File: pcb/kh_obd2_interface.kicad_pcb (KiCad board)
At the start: 2 copper layers, 35 parts, among them J1 OBD2, J2 CAN, Q201 CSD18540Q5B, U1 STM32G0B1RET6, U201 LM74500-Q1, U202 TVS2700DRV, U3 TPSM33620S5QRDNRQ1, U301 TCAN3403-Q1, U4 LM1117-Q1-3.3

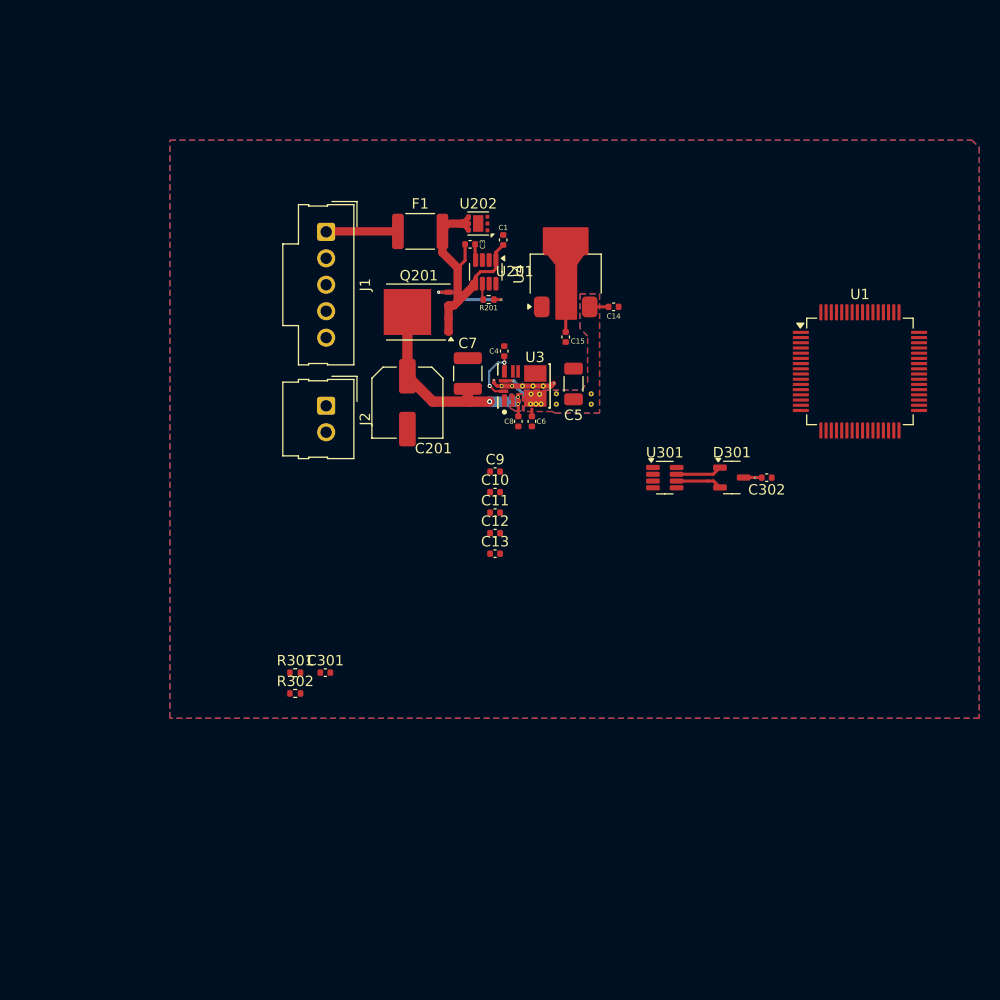
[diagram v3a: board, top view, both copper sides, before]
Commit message: add transceivers, routing, drc
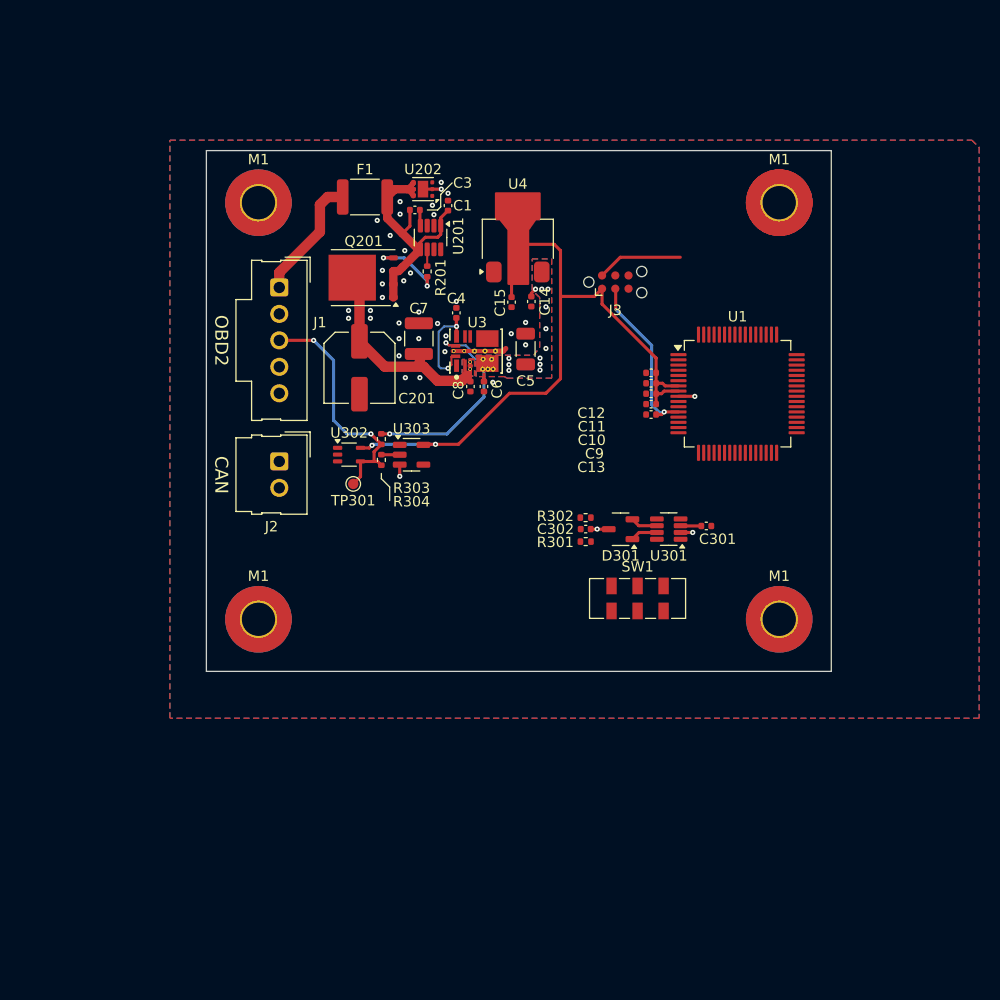
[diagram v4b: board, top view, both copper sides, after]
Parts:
- removed the ? at (54.5, 39.4)
- removed the ? at (51.1, 39.4)
- removed the ? at (54.5, 38.4)
- removed the ? at (51.1, 38.4)
- added ?: , , F.Cu at (72.5, 20.0)
- added J3: TC2030, Connector:Tag-Connect_TC2030-IDC-NL_2x03_P1.27mm_Vertical, F.Cu at (56.8, 27.6)
- added M1: MountingHole_3.2mm_M3_Pad_TopBottom, MountingHole:MountingHole_3.2mm_M3_Pad_TopBottom, F.Cu at (72.5, 60.0)
- added M1: MountingHole_3.2mm_M3_Pad_TopBottom, MountingHole:MountingHole_3.2mm_M3_Pad_TopBottom, F.Cu at (22.5, 60.0)
- added M1: MountingHole_3.2mm_M3_Pad_TopBottom, MountingHole:MountingHole_3.2mm_M3_Pad_TopBottom, F.Cu at (22.5, 20.0)
- added M1: MountingHole_3.2mm_M3_Pad_TopBottom, MountingHole:MountingHole_3.2mm_M3_Pad_TopBottom, F.Cu at (72.5, 20.0)
- added R303: 510r, Resistor_SMD:R_0402_1005Metric, F.Cu at (34.3, 42.7)
- added R304: 33r, Resistor_SMD:R_0402_1005Metric, F.Cu at (34.3, 44.7)
- added SW1: TermSw, Button_Switch_SMD:SW_DPDT_CK_JS202011JCQN, F.Cu at (58.9, 58.0)
- added TP301: HLine, TestPoint:TestPoint_Pad_D1.0mm, F.Cu at (31.6, 47.0)
- added U302: 74LVC1G07, Package_TO_SOT_SMD:Texas_R-PDSO-G5_DCK-5, F.Cu at (31.2, 44.2)
- added U303: SN74LV1T34DBV, Package_TO_SOT_SMD:SOT-23-5, F.Cu at (37.2, 44.2)
- moved C301 39.2 mm to (65.5, 51.0), turned to 180 degrees
- moved R302 32.6 mm to (53.9, 50.2)
- moved R301 30.6 mm to (53.9, 52.5), turned to 180 degrees
- moved C12 21.5 mm to (60.2, 36.3), turned to 180 degrees
- moved C13 20.1 mm to (60.2, 40.3)
- moved C11 19.5 mm to (60.2, 37.3), turned to 180 degrees
- moved C302 18.1 mm to (53.9, 51.3), turned to 0 degrees
- moved C10 17.7 mm to (60.2, 38.3), turned to 180 degrees
- moved C9 16.3 mm to (60.2, 39.3), turned to 180 degrees
- moved U1 11.9 mm to (68.5, 38.3)
- moved D301 11.8 mm to (57.3, 51.4), turned to 180 degrees
- moved C14 7.92 mm to (48.7, 29.5), turned to -90 degrees
- moved J2 6.98 mm to (24.5, 44.8)
- moved J1 6.98 mm to (24.5, 28.1)
- moved R201 6.49 mm to (38.7, 26.6), turned to 90 degrees
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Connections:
- net /MCU/MCU_NRST renamed /Connectors/MCU_NRST
- net /Transceivers/RX renamed /MCU/RX
- net /Transceivers/STB renamed /MCU/STB
- net /Transceivers/TX renamed /MCU/TX
- C15 pad 1: +3.3V -> +3V3
- C3 pad 1: +BATT_FUSED -> /Power/BATT_FUSED
- C301 pad 2: +3.3V -> +3V3
- J2 pad 1: unconnected-(J2-Pin_1-Pad1) -> /Connectors/CAN1.H
- J2 pad 2: unconnected-(J2-Pin_2-Pad2) -> /Connectors/CAN1.L
- R301 pad 2: Net-(C302-Pad1) -> Net-(R301-Pad2)
- R302 pad 1: Net-(C302-Pad1) -> Net-(R302-Pad1)
- U1 pad 45: /MCU/MCU_SWDIO -> /Connectors/MCU_SWDIO
- U1 pad 46: /MCU/MCU_SWCLK_BOOT0 -> /Connectors/MCU_SWCLK_BOOT0
- U201 pad 1: +BATT_FUSED -> /Power/BATT_FUSED
- U301 pad 3: +3.3V -> +3V3
- U4 pad 2: +3.3V -> +3V3
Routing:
- net +3V3: track 0.00 -> 68.8 mm, vias 0 -> 2
- net /Connectors/H Line: track 0.00 -> 23.7 mm, vias 0 -> 2
- net /Connectors/MCU_NRST: track 0.00 -> 16.4 mm, vias 0 -> 2
- net +5V: track 6.21 -> 21.0 mm, vias 1 -> 14
- net /Connectors/MCU_SWDIO: track 0.00 -> 8.23 mm
- net +BATT: track 6.91 -> 12.1 mm
- net +3.3V: track 5.12 -> 0.00 mm
- net GND: track 8.42 -> 12.4 mm, vias 3 -> 38
- net Net-(U3-MODE/SYNC): track 6.21 -> 9.67 mm
- net /Transceivers/CAN1.L: track 4.42 -> 2.60 mm
- net /Transceivers/CAN1.H: track 4.43 -> 2.61 mm
- net Net-(U303-A): track 0.00 -> 1.77 mm
- net /Power/BATT_FUSED: track 26.0 -> 25.2 mm
- net +12V: track 20.4 -> 20.8 mm, vias 1 -> 0
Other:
- board outline added: 60 x 50 mm
- board text added: "CAN"
- board text added: "OBD2"

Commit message: busses are hard
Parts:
- added J3: USB-C 2.0, Connector_USB:USB_C_Receptacle_GCT_USB4105-xx-A_16P_TopMnt_Horizontal, F.Cu at (60.3, 18.7)
- added J4: RTC_BAT, Connector_Molex:Molex_PicoBlade_53047-0210_1x02_P1.25mm_Vertical, F.Cu at (72.8, 51.2)
- added R401: 5.1k, Resistor_SMD:R_0402_1005Metric, F.Cu at (61.8, 24.5)
- added R402: 5.1k, Resistor_SMD:R_0402_1005Metric, F.Cu at (58.8, 24.5)
- added SW2: SW_SPDT, Connector_PinHeader_2.54mm:PinHeader_1x03_P2.54mm_Vertical_SMD_Pin1Left, F.Cu at (47.6, 27.7)
- moved J_SWD1 16.3 mm to (73.0, 26.7)
- moved C15 13.1 mm to (53.0, 18.0), turned to 90 degrees
- moved C14 8.77 mm to (42.7, 23.1)
- moved SW1 5.40 mm to (53.5, 57.3)
- moved C5 3.36 mm to (47.7, 37.4), turned to 90 degrees
- moved U4 3.16 mm to (47.7, 20.4), turned to 0 degrees
- renumbered J3 to J_SWD1
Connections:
- net /MCU/KL_UART.RX renamed /MCU/KLINE.RX
- net /MCU/KL_UART.TX renamed /MCU/KLINE.TX
- C5 pad 2: +5V -> /Power/CAR_5V
- C6 pad 2: +5V -> /Power/CAR_5V
- D301 pad 1: /Transceivers/CAN1.H -> /Connectors/H_+
- D301 pad 2: /Transceivers/CAN1.L -> /Connectors/L_-
- J2 pad 1: /Connectors/CAN1.H -> /Connectors/H_+
- J2 pad 2: /Connectors/CAN1.L -> /Connectors/L_-
- R301 pad 1: /Transceivers/CAN1.H -> /Connectors/H_+
- R302 pad 2: /Transceivers/CAN1.L -> /Connectors/L_-
- U1 pad 19: /MCU/HL_UART.TX -> /MCU/HLINE.TX
- U1 pad 20: /MCU/HL_UART.RX -> /MCU/HLINE.RX
- U1 pad 40: unconnected-(U1-PD8-Pad40) -> /MCU/TX
- U1 pad 41: unconnected-(U1-PD9-Pad41) -> /MCU/RX
- U1 pad 43: /MCU/USB1.DM -> /Connectors/DN
- U1 pad 44: /MCU/USB1.DP -> /Connectors/DP
- U1 pad 6: /MCU/RTC_VBAT -> /Connectors/RTC_VBAT
- U3 pad 4: +5V -> /Power/CAR_5V
- U3 pad 9: +5V -> /Power/CAR_5V
- U301 pad 6: /Transceivers/CAN1.L -> /Connectors/L_-
- U301 pad 7: /Transceivers/CAN1.H -> /Connectors/H_+
- U302 pad 2: /Transceivers/HL_UART.TX -> /MCU/HLINE.TX
- U303 pad 4: /Transceivers/HL_UART.RX -> /MCU/HLINE.RX
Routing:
- net /Connectors/DN: track 0.00 -> 31.7 mm
- net /Connectors/DP: track 0.00 -> 28.7 mm, vias 0 -> 2
- net /Connectors/RTC_VBAT: track 0.00 -> 20.6 mm
- net /Power/CAR_5V: track 0.00 -> 19.8 mm, vias 0 -> 2
- net /Connectors/USB_5V: track 0.00 -> 19.3 mm, vias 0 -> 2
- net +5V: track 21.0 -> 1.82 mm, vias 14 -> 0
- net +3V3: track 68.8 -> 51.3 mm, vias 2 -> 3
- net /Connectors/MCU_NRST: track 16.4 -> 2.25 mm, vias 2 -> 1
- net /Connectors/MCU_SWDIO: track 8.23 -> 0.00 mm
- net /Connectors/H_+: track 0.00 -> 7.20 mm
- net /Connectors/L_-: track 0.00 -> 5.97 mm
- net /Transceivers/CAN1.H: track 2.61 -> 0.00 mm
- net /Transceivers/CAN1.L: track 2.60 -> 0.00 mm
- net Net-(J3-CC2): track 0.00 -> 1.71 mm
- net Net-(J3-CC1): track 0.00 -> 1.71 mm
- added copper zone on B.Cu, net /Power/CAR_5V
- added copper zone on F.Cu, net /Power/CAR_5V
- removed copper zone on B.Cu, net +5V
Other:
- board text added: "CAR"
- board text added: "USB"

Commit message: Add TLIN2027, placement, DRC fixes, routing
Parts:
- removed ?: , 
- removed SW1: TermSw, Button_Switch_SMD:SW_DPDT_CK_JS202011JCQN
- added JP1: SolderJumper_2_Open, Jumper:SolderJumper-2_P1.3mm_Open_RoundedPad1.0x1.5mm, F.Cu at (52.0, 91.7)
- added JP2: SolderJumper_2_Open, Jumper:SolderJumper-2_P1.3mm_Open_RoundedPad1.0x1.5mm, F.Cu at (52.1, 85.8)
- added R305: 5.1k, Resistor_SMD:R_0402_1005Metric, F.Cu at (42.9, 43.8)
- added U2: TLIN2027-Q1, Package_SO:SOIC-8_3.9x4.9mm_P1.27mm, F.Cu at (48.1, 44.4)
- moved C301 37.4 mm to (63.6, 88.4)
- moved R301 37.4 mm to (52.1, 89.9)
- moved R302 37.4 mm to (52.1, 87.6)
- moved C302 37.4 mm to (52.1, 88.7)
- moved U301 37.4 mm to (60.0, 88.7)
- moved D301 30.8 mm to (26.6, 52.7), turned to -90 degrees
- moved TP301 1.49 mm to (33.0, 46.5)
- turned R401 to 90 degrees
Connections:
- net /MCU/HLINE.RX renamed /Communications/HLINE.RX
- net /MCU/HLINE.TX renamed /Communications/HLINE.TX
- net /MCU/RX renamed /Communications/RX
- net /MCU/STB renamed /Communications/STB
- net /MCU/TX renamed /Communications/TX
- D301 pad 1: /Connectors/H_+ -> /Communications/H_+
- D301 pad 2: /Connectors/L_- -> /Communications/L_-
- J2 pad 1: /Connectors/H_+ -> /Communications/H_+
- J2 pad 2: /Connectors/L_- -> /Communications/L_-
- R301 pad 1: /Connectors/H_+ -> Net-(JP1-B)
- R301 pad 2: Net-(R301-Pad2) -> Net-(C302-Pad1)
- R302 pad 1: Net-(R302-Pad1) -> Net-(C302-Pad1)
- R302 pad 2: /Connectors/L_- -> Net-(JP2-A)
- U1 pad 25: /MCU/KLINE.TX -> /Communications/KLINE.TX
- U1 pad 26: /MCU/KLINE.RX -> /Communications/KLINE.RX
- U301 pad 6: /Connectors/L_- -> /Communications/L_-
- U301 pad 7: /Connectors/H_+ -> /Communications/H_+
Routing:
- net /Connectors/K Line: track 0.00 -> 33.0 mm, vias 0 -> 1
- net /Communications/HLINE.RX: track 0.00 -> 30.4 mm, vias 0 -> 2
- net /Communications/KLINE.RX: track 0.00 -> 28.6 mm, vias 0 -> 2
- net /Communications/KLINE.TX: track 0.00 -> 27.4 mm, vias 0 -> 2
- net +5V: track 1.82 -> 28.7 mm, vias 0 -> 2
- net /Power/CAR_5V: track 19.8 -> 5.79 mm, vias 2 -> 1
- net /Communications/HLINE.TX: track 0.00 -> 11.6 mm, vias 0 -> 1
- net /Communications/H_+: track 0.00 -> 8.00 mm
- net /Communications/L_-: track 0.00 -> 8.00 mm
- net +3V3: track 51.3 -> 59.1 mm
- net /Connectors/H_+: track 7.20 -> 0.00 mm
- net /Connectors/L_-: track 5.97 -> 0.00 mm
- net Net-(C302-Pad1): track 0.00 -> 2.30 mm
- net Net-(U2-~{EN}): track 0.00 -> 2.26 mm
- net GND: track 12.4 -> 14.3 mm, vias 38 -> 68

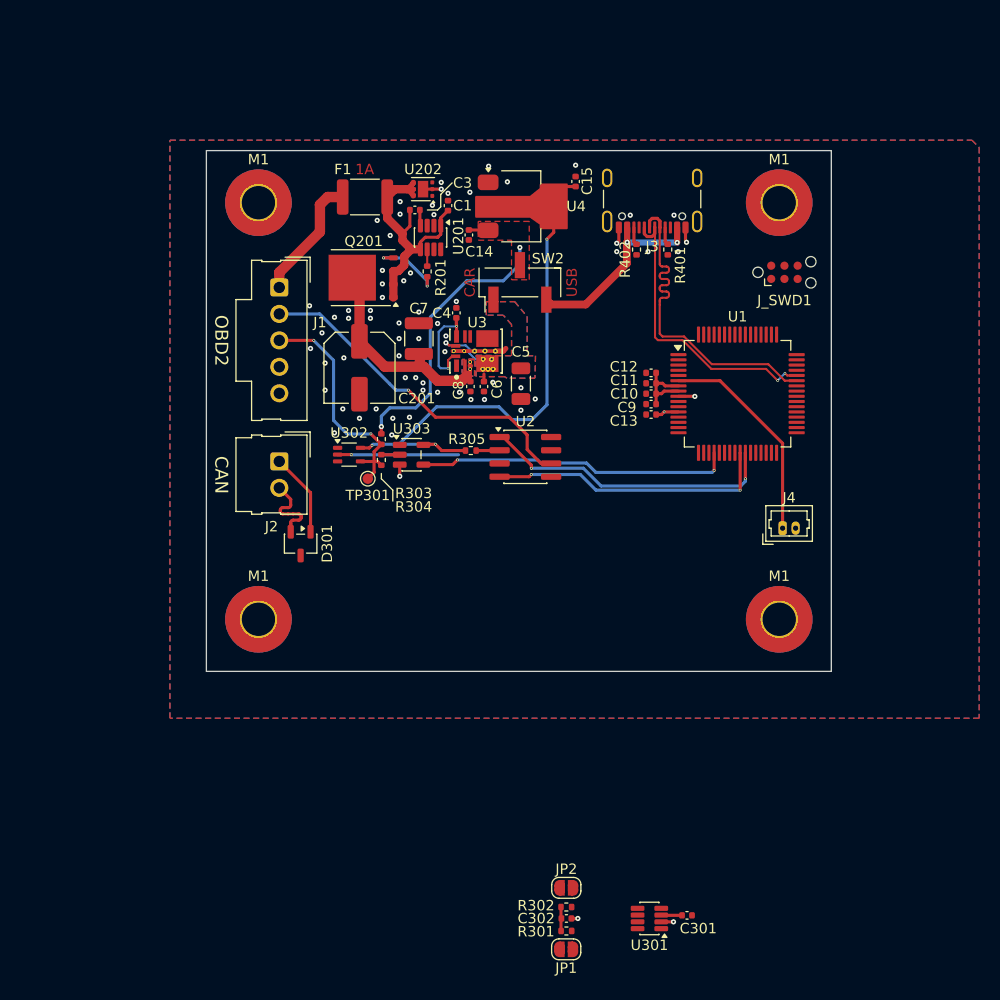
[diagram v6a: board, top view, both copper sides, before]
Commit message: CAN/mcu placement/routing
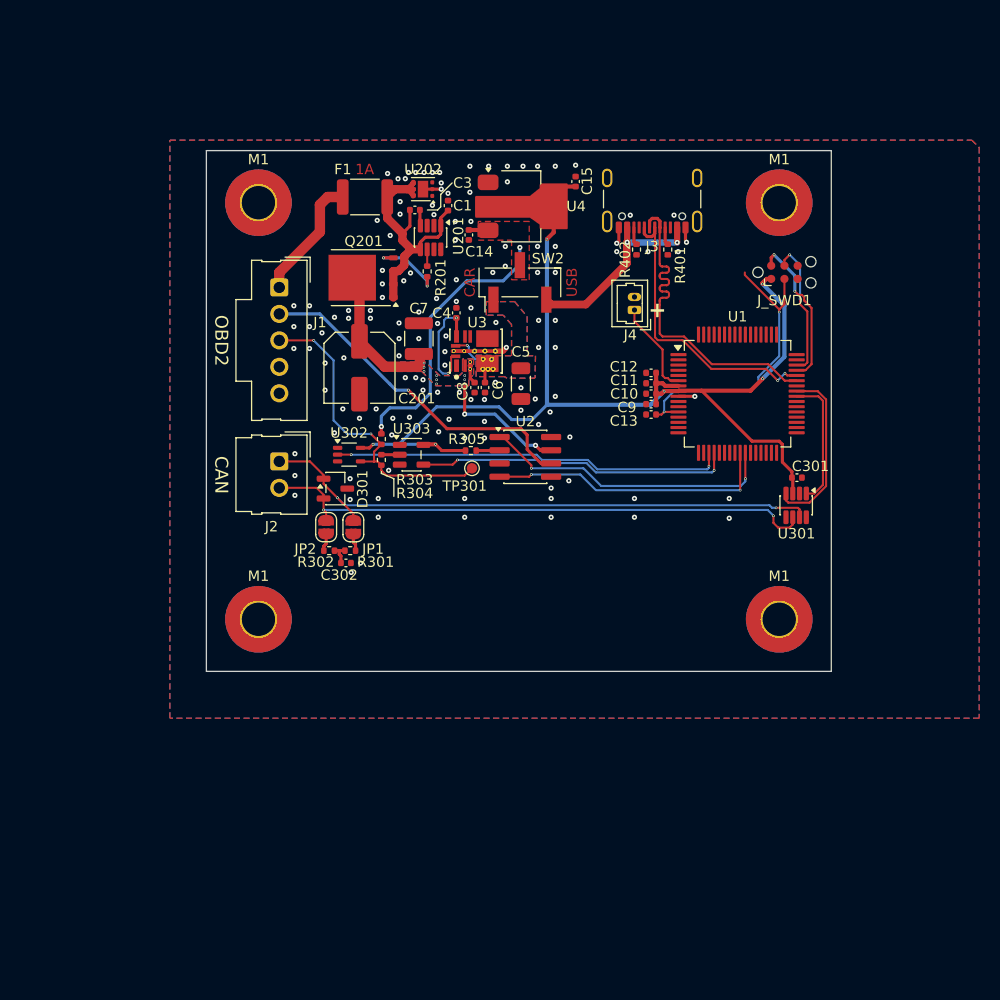
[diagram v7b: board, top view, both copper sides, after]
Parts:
- moved JP1 45.4 mm to (31.6, 51.2), turned to -90 degrees
- moved C301 43.3 mm to (74.2, 46.4)
- moved U301 42.1 mm to (74.1, 49.1), turned to -90 degrees
- moved R301 42.0 mm to (31.3, 53.4)
- moved JP2 41.6 mm to (29.0, 51.1), turned to 90 degrees
- moved R302 41.1 mm to (29.3, 53.4), turned to 180 degrees
- moved C302 40.2 mm to (30.9, 54.6)
- moved J4 25.3 mm to (58.6, 30.3), turned to 90 degrees
- moved TP301 10.0 mm to (43.0, 45.5)
- moved D301 6.25 mm to (29.9, 47.5), turned to 0 degrees
- moved C8 0.41 mm to (43.2, 37.8)
- moved C6 0.14 mm to (44.2, 37.8)
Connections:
- net /Communications/H_+ renamed /Communications/CAN.P
- net /Communications/L_- renamed /Communications/CAN.N
- U2 pad 7: unconnected-(U2-VBAT-Pad7) -> +12V
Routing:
- net /Communications/CAN.P: track 8.00 -> 55.9 mm, vias 0 -> 2
- net /Communications/CAN.N: track 8.00 -> 54.1 mm, vias 0 -> 2
- net +3V3: track 59.1 -> 104.4 mm, vias 3 -> 6
- net /Connectors/MCU_NRST: track 2.25 -> 29.0 mm, vias 1 -> 2
- net /Communications/HLINE.TX: track 11.6 -> 37.7 mm, vias 1 -> 2
- net /Communications/RX: track 0.00 -> 16.7 mm
- net /Connectors/MCU_SWDIO: track 0.00 -> 15.0 mm, vias 0 -> 2
- net /Connectors/MCU_SWCLK_BOOT0: track 0.00 -> 13.4 mm, vias 0 -> 2
- net /Communications/TX: track 0.00 -> 12.7 mm
- net /Connectors/RTC_VBAT: track 20.6 -> 9.35 mm
- net /Connectors/H Line: track 23.3 -> 31.1 mm
- net +12V: track 20.8 -> 28.5 mm, vias 0 -> 11
- net GND: track 14.3 -> 11.5 mm, vias 68 -> 131
- net Net-(JP2-A): track 0.00 -> 1.70 mm
- net Net-(JP1-B): track 0.00 -> 1.69 mm
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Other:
- board text added: "+"

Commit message: diff skew fixes, routing cleanups
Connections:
- C11 pad 2: Net-(C11-Pad2) -> GND
- C12 pad 2: Net-(C11-Pad2) -> GND
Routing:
- net GND: track 11.5 -> 16.7 mm, vias 131 -> 141
- net /Connectors/DN: track 31.7 -> 30.2 mm
